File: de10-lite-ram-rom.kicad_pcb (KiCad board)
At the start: 2 copper layers, 52.1 x 33 mm, 8 parts, among them J6 DE10-Lite GPIO, U1 AS6C4008A-55ZIN, U2 SST39LF040

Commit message: Final version
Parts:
- removed J6: DE10-Lite GPIO, Connector_PinSocket_2.54mm:PinSocket_2x20_P2.54mm_Vertical
- added G***: LOGO, Logos:asian_tiger, F.Cu at (154.7, 98.9)
- added J1: DE10-Lite_GPIO_Header, Connector_PinSocket_2.54mm:PinSocket_2x20_P2.54mm_Horizontal, F.Cu at (131.3, 115.1)
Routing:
- net VCC: track 115.6 -> 123.9 mm
- net /A1: track 38.7 -> 40.7 mm
- net /RAM_~CE: track 18.6 -> 20.3 mm
- net /D6: track 35.4 -> 37.0 mm
- net /A18: track 66.2 -> 67.4 mm
- net /D2: track 41.1 -> 42.3 mm
- net GND: track 10.1 -> 9.76 mm, vias 10 -> 13
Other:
- board size 52.1 x 33 mm -> 51.3 x 33.5 mm
- net class Power: trace_width 0.4064 -> 0.508; via_dia 0.8128 -> 1.016; via_drill 0.4064 -> 0.508
- board text added: "1"
- board text added: "3V3"
- board text added: "5V"
- board text added: "A0"
- board text added: "A10"
- board text added: "A11"
- board text added: "A12"
- board text added: "A13"
- board text added: "A14"
- board text added: "A16"
- board text added: "A18"
- board text added: "A2"
- board text added: "A3"
- board text added: "A4"
- board text added: "A5"
- board text added: "A7"
- board text added: "A9"
- board text added: "D0"
- board text added: "D1"
- board text added: "D2"
- board text added: "D3"
- board text added: "D4"
- board text added: "D5"
- board text added: "D6"
- board text added: "D7"
- board text added: "DE10-Lite 512K SRAM/Flash ROM Board version 1.0 by Hyiger Designs"
- board text added: "GND"
- board text added: "~A15"
- board text added: "~A17"
- board text added: "~RAM"
- board text added: "~RD"
- board text added: "~ROM"
- board text added: "~WR"
- board text added: "ø"

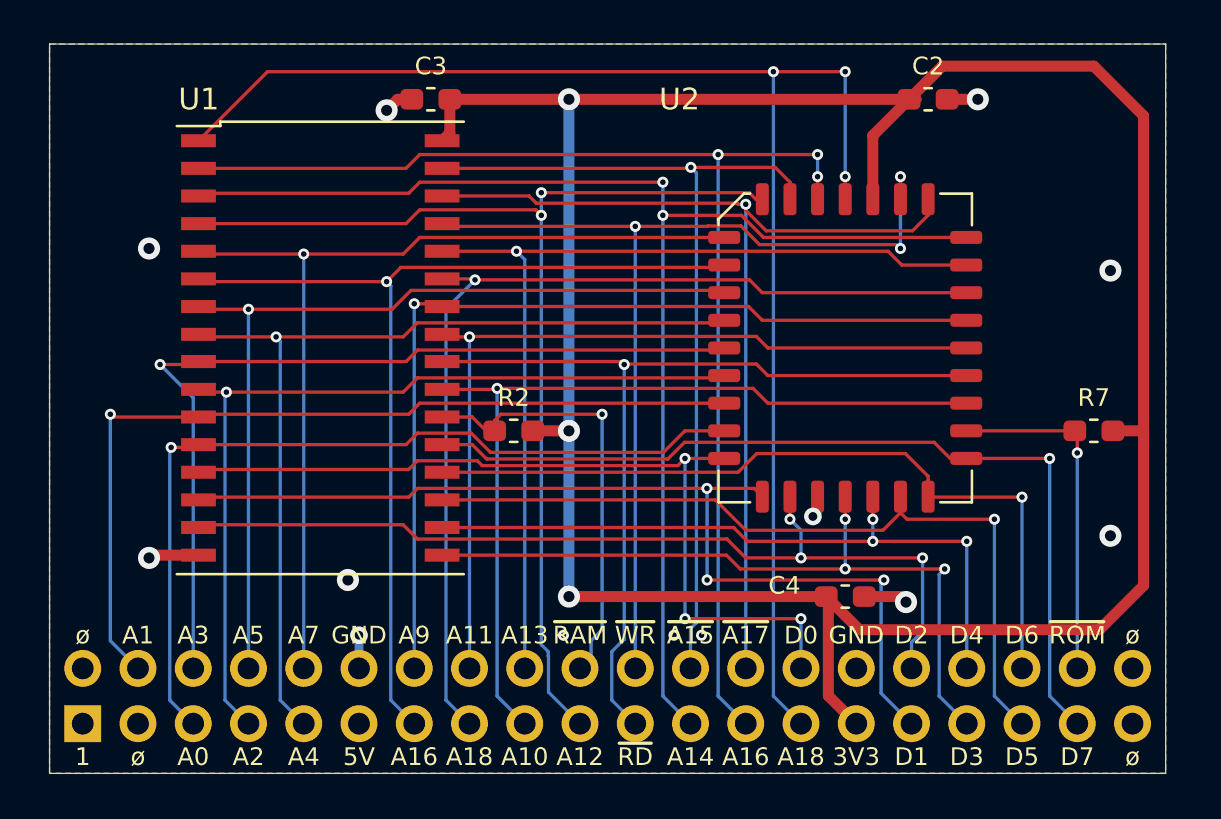
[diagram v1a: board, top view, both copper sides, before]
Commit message: removed pullups
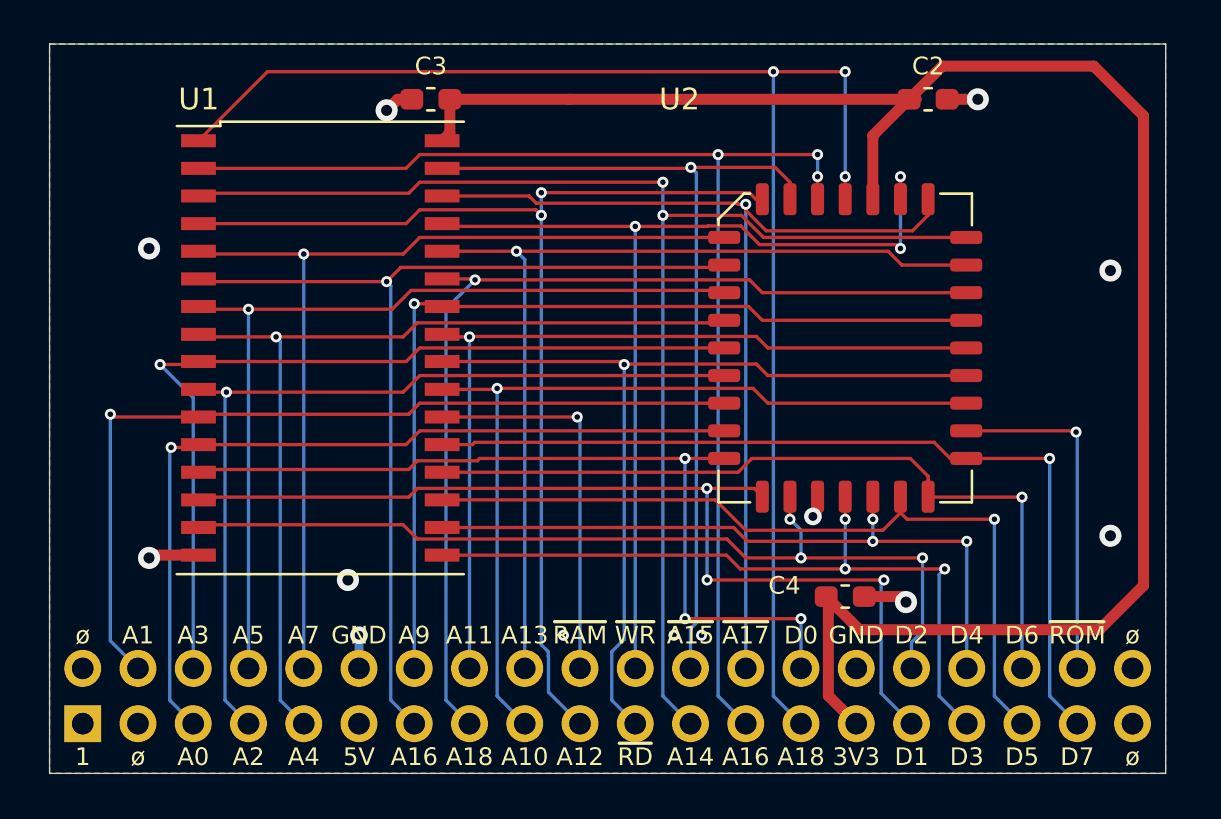
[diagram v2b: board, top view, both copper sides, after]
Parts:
- removed R2, R7: 10K, Resistor_SMD:R_0603_1608Metric_Pad1.05x0.95mm_HandSolder
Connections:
- J1 pad 1: (no net) -> Net-(J1-Pad1)
- J1 pad 11: (no net) -> +5V
- J1 pad 2: (no net) -> Net-(J1-Pad2)
- J1 pad 3: (no net) -> Net-(J1-Pad3)
- J1 pad 39: (no net) -> Net-(J1-Pad39)
- J1 pad 40: (no net) -> Net-(J1-Pad40)
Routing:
- net VCC: track 123.9 -> 85.9 mm, vias 3 -> 0
- net /RAM_~CE: track 20.3 -> 17.8 mm
- net /A0: track 39.6 -> 38.9 mm
- net /D7: track 41.5 -> 41.0 mm
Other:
- board text added: "DE10-Lite 512K SRAM/Flash ROM Board version 1.1 by Hyiger Designs"
- board text removed: "DE10-Lite 512K SRAM/Flash ROM Board version 1.0 by Hyiger Designs"
